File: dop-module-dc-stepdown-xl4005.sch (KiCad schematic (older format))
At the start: 13 parts, among them J101 Conn_01x02, J102 Conn_01x02, U101 XL4005

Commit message: compact layout in progress
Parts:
- added F102, F103, F104: 1A, Fuse:Fuse_1206_3216Metric_Pad1.42x1.75mm_HandSolder, symbol Device:Fuse_Small
- D101: symbol Device:D_Schottky_Small_ALT -> Device:D_Schottky_AKA
- F101: value 2A -> 1A
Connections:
- net GND: now also D101.1 (A), D101.3 (A); no longer D101.2 (A)
- net at F101.2, U101.3 (SW): now also F102.2, F103.2, F104.2
- net at F101.1, L101.1: now also D101.2 (K), F102.1, F103.1, F104.1; no longer D101.1 (K)
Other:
- moved on the sheet: C104, J102, L101
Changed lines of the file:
@@
 $EndComp
 $Comp
-L Device:D_Schottky_Small_ALT D101
+L Device:D_Schottky_AKA D101
 U 1 1 61EAF8CB
-P 5300 5000
-F 0 "D101" V 5200 5000 50  0000 L CNN
-F 1 "50WQ03" V 5400 5000 50  0000 L CNN
-F 2 "Package_TO_SOT_SMD:TO-252-2" V 5300 5000 50  0001 C CNN
-F 3 "~" V 5300 5000 50  0001 C CNN
-	1    5300 5000
+P 5600 5000
+F 0 "D101" V 5550 5100 50  0000 L CNN
+F 1 "50WQ03" V 5650 5100 50  0000 L CNN
+F 2 "Package_TO_SOT_SMD:TO-252-2" V 5600 5000 50  0001 C CNN
+F 3 "~" V 5600 5000 50  0001 C CNN
+	1    5600 5000
 	0    1    1    0
 $EndComp
@@
 L Device:L_Small L101
 U 1 1 61EAFC29
-P 5700 4750
-F 0 "L101" V 5800 4700 50  0000 L CNN
-F 1 "33uH 5A" V 5650 4600 50  0000 L CNN
-F 2 "Inductor_SMD:L_10.4x10.4_H4.8" H 5700 4750 50  0001 C CNN
-F 3 "~" H 5700 4750 50  0001 C CNN
-	1    5700 4750
+P 6000 4750
+F 0 "L101" V 6100 4700 50  0000 L CNN
+F 1 "33uH 5A" V 5950 4600 50  0000 L CNN
+F 2 "Inductor_SMD:L_10.4x10.4_H4.8" H 6000 4750 50  0001 C CNN
+F 3 "~" H 6000 4750 50  0001 C CNN
+	1    6000 4750
 	0    -1   -1   0
 $EndComp
@@
 L Connector_Generic:Conn_01x02 J102
 U 1 1 61EBB426
-P 7100 4950
-F 0 "J102" H 7100 5050 50  0000 C CNN
-F 1 "Conn_01x02" H 7100 4750 50  0000 C CNN
-F 2 "castellated:castellated_2x4_fingers" H 7100 4950 50  0001 C CNN
-F 3 "~" H 7100 4950 50  0001 C CNN
-	1    7100 4950
+P 7400 4950
+F 0 "J102" H 7400 5050 50  0000 C CNN
+F 1 "Conn_01x02" H 7400 4750 50  0000 C CNN
+F 2 "castellated:castellated_2x4_fingers" H 7400 4950 50  0001 C CNN
+F 3 "~" H 7400 4950 50  0001 C CNN
+	1    7400 4950
 	1    0    0    -1
 $EndComp
@@
 	2000 5150 2400 5150
 Wire Wire Line
-	6700 4750 6700 4950
-Wire Wire Line
-	6700 4950 6900 4950
-Wire Wire Line
-	6800 5250 6800 5050
-Wire Wire Line
-	6800 5050 6900 5050
+	7000 4750 7000 4950
+Wire Wire Line
+	7000 4950 7200 4950
+Wire Wire Line
+	7100 5250 7100 5050
+Wire Wire Line
+	7100 5050 7200 5050
 $Comp
 L power:GND #PWR0106
 U 1 1 61EBEAC9
-P 6600 5250
-F 0 "#PWR0106" H 6600 5000 50  0001 C CNN
-F 1 "GND" H 6600 5100 50  0000 C CNN
-F 2 "" H 6600 5250 50  0001 C CNN
-F 3 "" H 6600 5250 50  0001 C CNN
-	1    6600 5250
-	1    0    0    -1
-$EndComp
-Connection ~ 6600 5250
-Wire Wire Line
-	6600 5250 6800 5250
+P 6900 5250
+F 0 "#PWR0106" H 6900 5000 50  0001 C CNN
+F 1 "GND" H 6900 5100 50  0000 C CNN
+F 2 "" H 6900 5250 50  0001 C CNN
+F 3 "" H 6900 5250 50  0001 C CNN
+	1    6900 5250
+	1    0    0    -1
+$EndComp
+Connection ~ 6900 5250
+Wire Wire Line
+	6900 5250 7100 5250
 $Comp
 L power:+5V #PWR0104
 U 1 1 61EBF25A
-P 6600 4750
-F 0 "#PWR0104" H 6600 4600 50  0001 C CNN
-F 1 "+5V" H 6600 4890 50  0000 C CNN
-F 2 "" H 6600 4750 50  0001 C CNN
-F 3 "" H 6600 4750 50  0001 C CNN
-	1    6600 4750
-	1    0    0    -1
-$EndComp
-Connection ~ 6600 4750
-Wire Wire Line
-	6600 4750 6700 4750
-Wire Wire Line
-	6100 4750 6100 4900
-Wire Wire Line
-	6100 4750 6600 4750
-Wire Wire Line
-	6100 5100 6100 5250
-Wire Wire Line
-	6100 5250 6600 5250
-Wire Wire Line
-	5300 4900 5300 4750
-Wire Wire Line
-	5300 4750 5600 4750
-Wire Wire Line
-	5800 4750 6100 4750
-Connection ~ 6100 4750
-Wire Wire Line
-	6100 5250 5300 5250
-Wire Wire Line
-	5300 5250 5300 5100
-Connection ~ 6100 5250
+P 6900 4750
+F 0 "#PWR0104" H 6900 4600 50  0001 C CNN
+F 1 "+5V" H 6900 4890 50  0000 C CNN
+F 2 "" H 6900 4750 50  0001 C CNN
+F 3 "" H 6900 4750 50  0001 C CNN
+	1    6900 4750
+	1    0    0    -1
+$EndComp
+Connection ~ 6900 4750
+Wire Wire Line
+	6900 4750 7000 4750
+Wire Wire Line
+	6400 4750 6400 4900
+Wire Wire Line
+	6400 4750 6900 4750
+Wire Wire Line
+	6400 5100 6400 5250
+Wire Wire Line
+	6400 5250 6900 5250
+Wire Wire Line
+	6100 4750 6400 4750
+Connection ~ 6400 4750
+Wire Wire Line
+	6400 5250 5700 5250
+Connection ~ 6400 5250
 $Comp
 L Device:CP1_Small C104
 U 1 1 61EC110D
-P 6100 5000
-F 0 "C104" H 6100 5100 50  0000 L CNN
-F 1 "470uF 50V" H 6100 4900 50  0000 L CNN
-F 2 "Capacitor_THT:CP_Radial_D12.5mm_P7.50mm" H 6100 5000 50  0001 C CNN
-F 3 "~" H 6100 5000 50  0001 C CNN
-	1    6100 5000
-	1    0    0    -1
-$EndComp
-Text Notes 5600 4500 0    50   ~ 0
+P 6400 5000
+F 0 "C104" H 6400 5100 50  0000 L CNN
+F 1 "470uF 50V" H 6400 4900 50  0000 L CNN
+F 2 "Capacitor_THT:CP_Radial_D12.5mm_P7.50mm" H 6400 5000 50  0001 C CNN
+F 3 "~" H 6400 5000 50  0001 C CNN
+	1    6400 5000
+	1    0    0    -1
+$EndComp
+Text Notes 5900 4500 0    50   ~ 0
 Power output and filtering
 $Comp
@@
 U 1 1 61EE40E9
 P 5000 4750
-F 0 "F101" H 5000 4650 50  0000 C CNN
-F 1 "2A" H 5000 4850 50  0000 C CNN
+F 0 "F101" H 5150 4700 50  0000 C CNN
+F 1 "1A" H 4900 4700 50  0000 C CNN
 F 2 "Fuse:Fuse_1206_3216Metric_Pad1.42x1.75mm_HandSolder" H 5000 4750 50  0001 C CNN
 F 3 "~" H 5000 4750 50  0001 C CNN
@@
 $EndComp
 Wire Wire Line
-	4600 4750 4900 4750
+	4600 4750 4700 4750
+$Comp
+L Device:Fuse_Small F102
+U 1 1 61EC3319
+P 5000 4850
+F 0 "F102" H 5150 4800 50  0000 C CNN
+F 1 "1A" H 4900 4800 50  0000 C CNN
+F 2 "Fuse:Fuse_1206_3216Metric_Pad1.42x1.75mm_HandSolder" H 5000 4850 50  0001 C CNN
+F 3 "~" H 5000 4850 50  0001 C CNN
+	1    5000 4850
+	-1   0    0    1
+$EndComp
+$Comp
+L Device:Fuse_Small F103
+U 1 1 61EC36A4
+P 5000 4950
+F 0 "F103" H 5150 4900 50  0000 C CNN
+F 1 "1A" H 4900 4900 50  0000 C CNN
+F 2 "Fuse:Fuse_1206_3216Metric_Pad1.42x1.75mm_HandSolder" H 5000 4950 50  0001 C CNN
+F 3 "~" H 5000 4950 50  0001 C CNN
+	1    5000 4950
+	-1   0    0    1
+$EndComp
+$Comp
+L Device:Fuse_Small F104
+U 1 1 61EC3B1F
+P 5000 5050
+F 0 "F104" H 5150 5000 50  0000 C CNN
+F 1 "1A" H 4900 5000 50  0000 C CNN
+F 2 "Fuse:Fuse_1206_3216Metric_Pad1.42x1.75mm_HandSolder" H 5000 5050 50  0001 C CNN
+F 3 "~" H 5000 5050 50  0001 C CNN
+	1    5000 5050
+	-1   0    0    1
+$EndComp
+Wire Wire Line
+	4700 4750 4700 4850
+Wire Wire Line
+	4700 5050 4900 5050
+Connection ~ 4700 4750
+Wire Wire Line
+	4700 4750 4900 4750
+Wire Wire Line
+	4900 4850 4700 4850
+Connection ~ 4700 4850
+Wire Wire Line
+	4700 4850 4700 4950
+Wire Wire Line
+	4900 4950 4700 4950
+Connection ~ 4700 4950
+Wire Wire Line
+	4700 4950 4700 5050
+Wire Wire Line
+	5300 5050 5300 4950
+Connection ~ 5300 4750
 Wire Wire Line
 	5100 4750 5300 4750
-Connection ~ 5300 4750
+Wire Wire Line
+	5100 5050 5300 5050
+Wire Wire Line
+	5100 4950 5300 4950
+Connection ~ 5300 4950
+Wire Wire Line
+	5300 4950 5300 4850
+Wire Wire Line
+	5100 4850 5300 4850
+Connection ~ 5300 4850
+Wire Wire Line
+	5300 4850 5300 4750
+Wire Wire Line
+	5700 5200 5700 5250
+Connection ~ 5700 5250
+Wire Wire Line
+	5700 5250 5600 5250
+Wire Wire Line
+	5600 5250 5600 5200
+Wire Wire Line
+	5300 4750 5600 4750
+Wire Wire Line
+	5600 4850 5600 4750
+Connection ~ 5600 4750
+Wire Wire Line
+	5600 4750 5900 4750
 $EndSCHEMATC

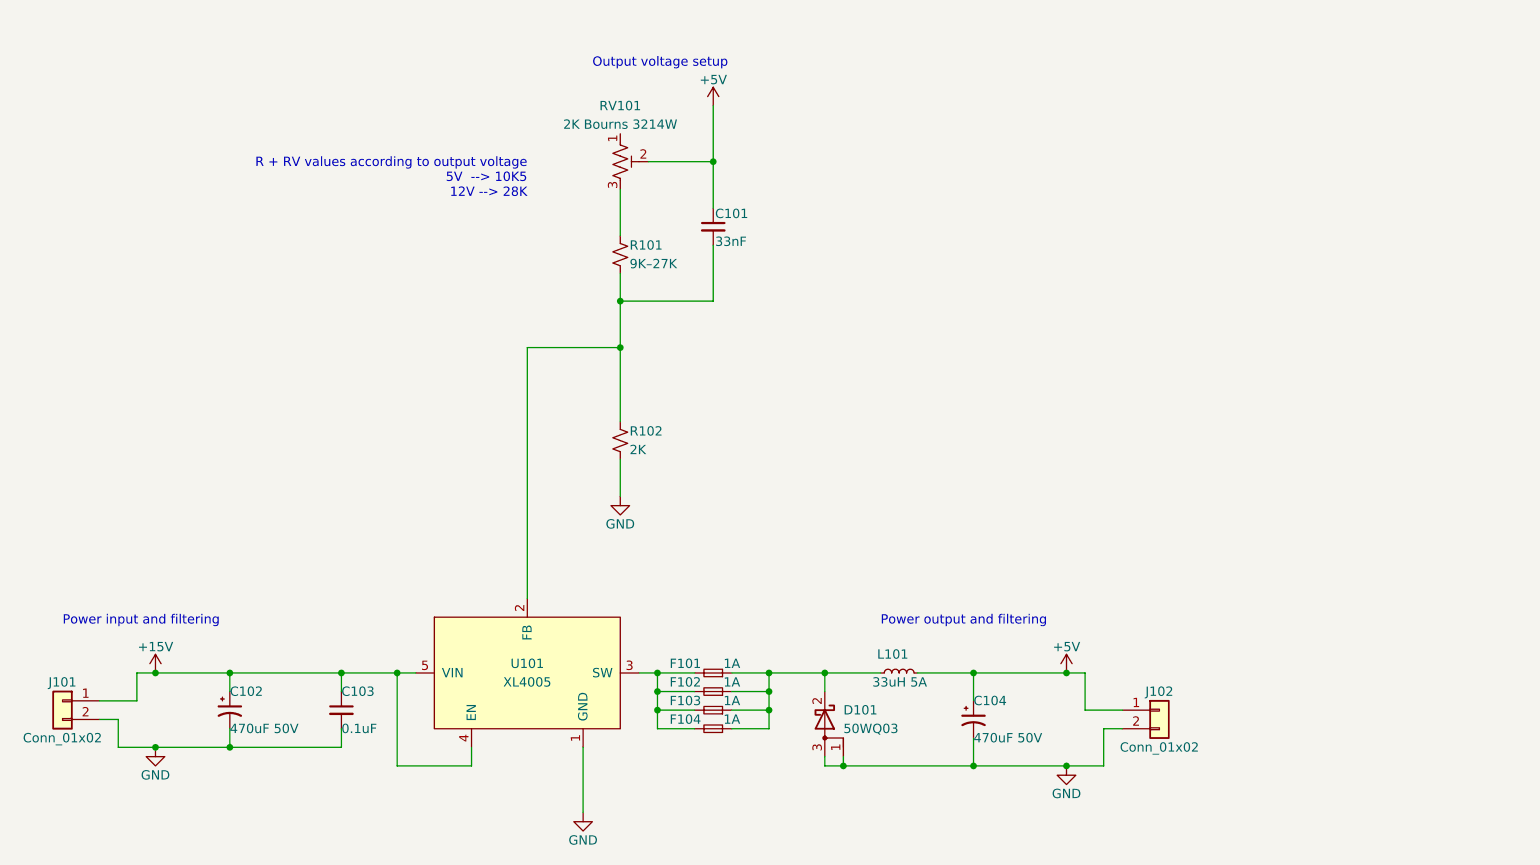
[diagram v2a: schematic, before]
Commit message: replace J101 and J102 by explicit 2x08 pin headers
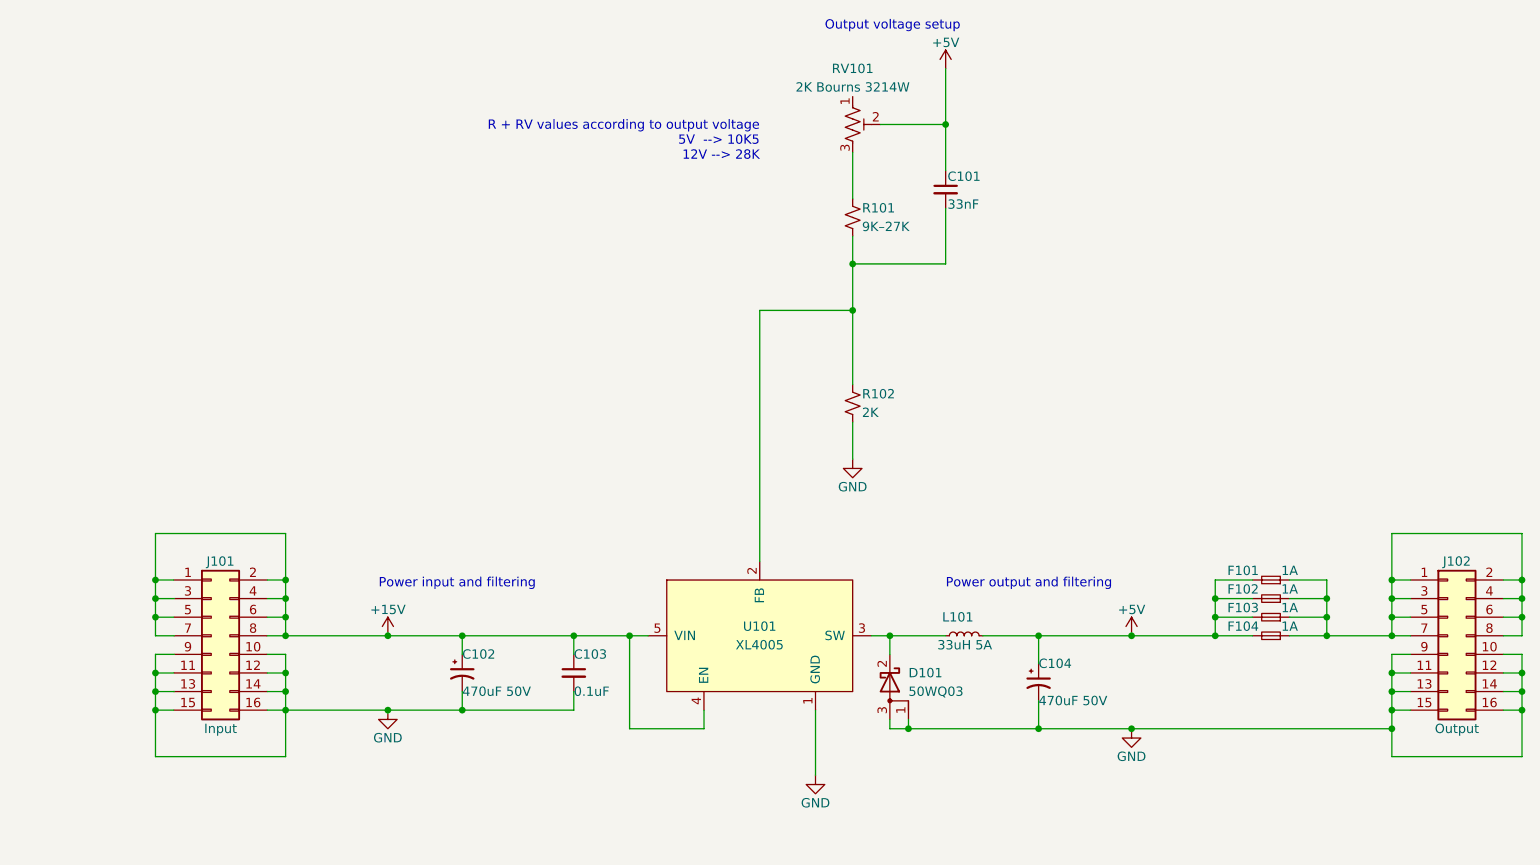
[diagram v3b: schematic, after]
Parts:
- removed J101, J102: Conn_01x02, castellated:castellated_2x4_fingers, symbol Connector_Generic:Conn_01x02
- added J101: Input, Connector_PinHeader_2.54mm:PinHeader_2x08_P2.54mm_Vertical, symbol Connector_Generic:Conn_02x08_Odd_Even
- added J102: Output, Connector_PinHeader_2.54mm:PinHeader_2x08_P2.54mm_Vertical, symbol Connector_Generic:Conn_02x08_Odd_Even
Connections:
- net +15V: now also J101.1 (Pin_1), J101.2 (Pin_2), J101.3 (Pin_3), J101.4 (Pin_4), J101.5 (Pin_5), J101.6 (Pin_6), J101.7 (Pin_7), J101.8 (Pin_8)
- net +5V: now also F101.2, F102.2, F103.2, F104.2
- net GND: now also J101.10 (Pin_10), J101.11 (Pin_11), J101.12 (Pin_12), J101.13 (Pin_13), J101.14 (Pin_14), J101.15 (Pin_15), J101.16 (Pin_16), J101.9 (Pin_9), J102.10 (Pin_10), J102.11 (Pin_11), J102.12 (Pin_12), J102.13 (Pin_13), J102.14 (Pin_14), J102.15 (Pin_15), J102.16 (Pin_16), J102.9 (Pin_9)
- net at F101.1, F102.1, F103.1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: now also J102.1 (Pin_1), J102.2 (Pin_2), J102.3 (Pin_3), J102.4 (Pin_4), J102.5 (Pin_5), J102.6 (Pin_6), J102.7 (Pin_7), J102.8 (Pin_8); no longer D101.2 (K), L101.1
- new net: D101.2 (K), L101.1, U101.3 (SW)
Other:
- moved on the sheet: C101, C102, C103, C104, D101, F101, F102, F103, F104, L101, R101, R102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

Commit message: complete rework
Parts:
- removed F101, F102, F103, F104: 1A, Fuse:Fuse_1206_3216Metric_Pad1.42x1.75mm_HandSolder, symbol Device:Fuse_Small
- removed J101: Input, Connector_PinHeader_2.54mm:PinHeader_2x08_P2.54mm_Vertical, symbol Connector_Generic:Conn_02x08_Odd_Even
- removed J102: Output, Connector_PinHeader_2.54mm:PinHeader_2x08_P2.54mm_Vertical, symbol Connector_Generic:Conn_02x08_Odd_Even
- added J101: V_IN, Connector_PinHeader_2.54mm:PinHeader_2x02_P2.54mm_Vertical, symbol Connector_Generic:Conn_02x02_Odd_Even
- added J102: GND_IN, Connector_PinHeader_2.54mm:PinHeader_2x02_P2.54mm_Vertical, symbol Connector_Generic:Conn_02x02_Odd_Even
- added J103: V_OUT, Connector_PinHeader_2.54mm:PinHeader_1x04_P2.54mm_Vertical, symbol Connector_Generic:Conn_01x04
- added J104: GND_OUT, Connector_PinHeader_2.54mm:PinHeader_1x04_P2.54mm_Vertical, symbol Connector_Generic:Conn_01x04
- C102, C104: footprint Capacitor_THT:CP_Radial_D12.5mm_P7.50mm -> Capacitor_THT:CP_Radial_D13.0mm_P5.00mm
- L101: footprint Inductor_SMD:L_10.4x10.4_H4.8 -> coilcraft_THT:CoilCraft_AGP2923
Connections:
- net +15V: now also J101.1 (Pin_1), J101.2 (Pin_2), J101.3 (Pin_3), J101.4 (Pin_4)
- net +5V: now also J103.1 (Pin_1), J103.2 (Pin_2), J103.3 (Pin_3), J103.4 (Pin_4)
- net GND: now also J102.1 (Pin_1), J102.2 (Pin_2), J102.3 (Pin_3), J102.4 (Pin_4), J104.1 (Pin_1), J104.2 (Pin_2), J104.3 (Pin_3), J104.4 (Pin_4)
- no-connect marks 0 -> 1

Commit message: add LCSC skus for generating bom
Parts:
- C101: LCSC (none) -> C318778
- C103: LCSC (none) -> C24497
- D101: LCSC (none) -> C222476
- R101: LCSC (none) -> C2984531
- R102: LCSC (none) -> C844028
- RV101: LCSC (none) -> C780202
- U101: LCSC (none) -> C73332
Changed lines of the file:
@@
 F 2 "Capacitor_SMD:C_1206_3216Metric_Pad1.33x1.80mm_HandSolder" H 6250 2150 50  0001 C CNN
 F 3 "~" H 6250 2150 50  0001 C CNN
+F 4 "C318778" H 6250 2150 50  0001 C CNN "LCSC"
 	1    6250 2150
 	1    0    0    -1
@@
 F 2 "Potentiometer_SMD:Potentiometer_Bourns_3214W_Vertical" H 5750 1800 50  0001 C CNN
 F 3 "~" H 5750 1800 50  0001 C CNN
+F 4 "C780202" H 5750 1800 50  0001 C CNN "LCSC"
 	1    5750 1800
 	1    0    0    -1
@@
 F 2 "Resistor_SMD:R_1206_3216Metric_Pad1.30x1.75mm_HandSolder" H 5750 2300 50  0001 C CNN
 F 3 "~" H 5750 2300 50  0001 C CNN
+F 4 "C2984531" H 5750 2300 50  0001 C CNN "LCSC"
 	1    5750 2300
 	1    0    0    -1
@@
 F 2 "Resistor_SMD:R_1206_3216Metric_Pad1.30x1.75mm_HandSolder" H 5750 3300 50  0001 C CNN
 F 3 "~" H 5750 3300 50  0001 C CNN
+F 4 "C844028" H 5750 3300 50  0001 C CNN "LCSC"
 	1    5750 3300
 	1    0    0    -1
@@
 F 2 "Package_TO_SOT_SMD:TO-252-2" V 5950 4800 50  0001 C CNN
 F 3 "~" V 5950 4800 50  0001 C CNN
+F 4 "C222476" V 5950 4800 50  0001 C CNN "LCSC"
 	1    5950 4800
 	0    1    1    0
@@
 F 2 "Capacitor_SMD:C_1206_3216Metric_Pad1.33x1.80mm_HandSolder" H 4250 4750 50  0001 C CNN
 F 3 "~" H 4250 4750 50  0001 C CNN
+F 4 "C24497" H 4250 4750 50  0001 C CNN "LCSC"
 	1    4250 4750
 	1    0    0    -1
@@
 F 2 "Package_TO_SOT_SMD:TO-263-5_TabPin3" H 5250 4550 50  0001 C CNN
 F 3 "https://datasheet.lcsc.com/lcsc/1808111512_XLSEMI-XL4005E1_C73332.pdf" H 5250 4550 50  0001 C CNN
+F 4 "C73332" H 5250 4550 50  0001 C CNN "LCSC"
 	1    5250 4550
 	1    0    0    -1
